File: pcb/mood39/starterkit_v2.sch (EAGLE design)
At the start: 19 parts, among them IC1 TINY85, IC2 LP2950

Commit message: new usb connector package
this will be puzzling not fun :-/
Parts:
- U$2: value USB_B -> USB_BS; device n39:USB_B -> n39:USB_BS
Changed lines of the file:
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@@
 <grid distance="0.1" unitdist="inch" unit="inch" style="lines" multiple="1" display="no" altdistance="0.01" altunitdist="inch" altunit="inch"/>
 <layers>
-<layer number="1" name="Top" color="4" fill="1" visible="no" active="no"/>
-<layer number="16" name="Bottom" color="1" fill="1" visible="no" active="no"/>
-<layer number="17" name="Pads" color="2" fill="1" visible="no" active="no"/>
-<layer number="18" name="Vias" color="2" fill="1" visible="no" active="no"/>
-<layer number="19" name="Unrouted" color="6" fill="1" visible="no" active="no"/>
-<layer number="20" name="Dimension" color="15" fill="1" visible="no" active="no"/>
-<layer number="21" name="tPlace" color="7" fill="1" visible="no" active="no"/>
-<layer number="22" name="bPlace" color="7" fill="1" visible="no" active="no"/>
-<layer number="23" name="tOrigins" color="15" fill="1" visible="no" active="no"/>
-<layer number="24" name="bOrigins" color="15" fill="1" visible="no" active="no"/>
-<layer number="25" name="tNames" color="7" fill="1" visible="no" active="no"/>
-<layer number="26" name="bNames" color="7" fill="1" visible="no" active="no"/>
-<layer number="27" name="tValues" color="7" fill="1" visible="no" active="no"/>
-<layer number="28" name="bValues" color="7" fill="1" visible="no" active="no"/>
+<layer number="1" name="Top" color="4" fill="1" visible="yes" active="no"/>
+<layer number="16" name="Bottom" color="1" fill="1" visible="yes" active="no"/>
+<layer number="17" name="Pads" color="2" fill="1" visible="yes" active="no"/>
+<layer number="18" name="Vias" color="2" fill="1" visible="yes" active="no"/>
+<layer number="19" name="Unrouted" color="6" fill="1" visible="yes" active="no"/>
+<layer number="20" name="Dimension" color="15" fill="1" visible="yes" active="no"/>
+<layer number="21" name="tPlace" color="7" fill="1" visible="yes" active="no"/>
+<layer number="22" name="bPlace" color="7" fill="1" visible="yes" active="no"/>
+<layer number="23" name="tOrigins" color="15" fill="1" visible="yes" active="no"/>
+<layer number="24" name="bOrigins" color="15" fill="1" visible="yes" active="no"/>
+<layer number="25" name="tNames" color="7" fill="1" visible="yes" active="no"/>
+<layer number="26" name="bNames" color="7" fill="1" visible="yes" active="no"/>
+<layer number="27" name="tValues" color="7" fill="1" visible="yes" active="no"/>
+<layer number="28" name="bValues" color="7" fill="1" visible="yes" active="no"/>
 <layer number="29" name="tStop" color="7" fill="3" visible="no" active="no"/>
 <layer number="30" name="bStop" color="7" fill="6" visible="no" active="no"/>
@@
 <layer number="35" name="tGlue" color="7" fill="4" visible="no" active="no"/>
 <layer number="36" name="bGlue" color="7" fill="5" visible="no" active="no"/>
-<layer number="37" name="tTest" color="7" fill="1" visible="no" active="no"/>
-<layer number="38" name="bTest" color="7" fill="1" visible="no" active="no"/>
+<layer number="37" name="tTest" color="7" fill="1" visible="yes" active="no"/>
+<layer number="38" name="bTest" color="7" fill="1" visible="yes" active="no"/>
 <layer number="39" name="tKeepout" color="4" fill="11" visible="no" active="no"/>
 <layer number="40" name="bKeepout" color="1" fill="11" visible="no" active="no"/>
@@
 <layer number="44" name="Drills" color="7" fill="1" visible="no" active="no"/>
 <layer number="45" name="Holes" color="7" fill="1" visible="no" active="no"/>
-<layer number="46" name="Milling" color="3" fill="1" visible="no" active="no"/>
-<layer number="47" name="Measures" color="7" fill="1" visible="no" active="no"/>
-<layer number="48" name="Document" color="7" fill="1" visible="no" active="no"/>
-<layer number="49" name="Reference" color="7" fill="1" visible="no" active="no"/>
-<layer number="51" name="tDocu" color="7" fill="1" visible="no" active="no"/>
-<layer number="52" name="bDocu" color="7" fill="1" visible="no" active="no"/>
+<layer number="46" name="Milling" color="3" fill="1" visible="yes" active="no"/>
+<layer number="47" name="Measures" color="7" fill="1" visible="yes" active="no"/>
+<layer number="48" name="Document" color="7" fill="1" visible="yes" active="no"/>
+<layer number="49" name="Reference" color="7" fill="1" visible="yes" active="no"/>
+<layer number="51" name="tDocu" color="7" fill="1" visible="yes" active="no"/>
+<layer number="52" name="bDocu" color="7" fill="1" visible="yes" active="no"/>
 <layer number="91" name="Nets" color="2" fill="1" visible="yes" active="yes"/>
 <layer number="92" name="Busses" color="1" fill="1" visible="yes" active="yes"/>
@@
 <part name="JP2" library="pinhead" deviceset="PINHD-1X1" device=""/>
 <part name="JP3" library="pinhead" deviceset="PINHD-1X1" device=""/>
-<part name="U$2" library="n39" deviceset="USB_B" device=""/>
+<part name="U$2" library="n39" deviceset="USB_B" device="S" value="USB_BS"/>
 </parts>
 <sheets>

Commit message: start routing
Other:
- moved on the sheet: JP2, JP3
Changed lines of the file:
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@@
 <instance part="S1" gate="S$1" x="73.66" y="50.8" rot="R270"/>
 <instance part="U$1" gate="G$1" x="-30.48" y="88.9" rot="R180"/>
-<instance part="JP2" gate="G$1" x="132.08" y="25.4"/>
-<instance part="JP3" gate="G$1" x="132.08" y="38.1"/>
+<instance part="JP2" gate="G$1" x="132.08" y="22.86"/>
+<instance part="JP3" gate="G$1" x="132.08" y="30.48"/>
 <instance part="U$2" gate="G$1" x="93.98" y="30.48"/>
 </instances>
@@
 </segment>
 <segment>
-<wire x1="106.68" y1="35.56" x2="116.84" y2="35.56" width="0.1524" layer="91"/>
-<label x="109.22" y="35.56" size="1.778" layer="95"/>
+<label x="129.54" y="40.64" size="1.778" layer="95"/>
+<wire x1="111.76" y1="40.64" x2="111.76" y2="35.56" width="0.1524" layer="91"/>
 <pinref part="U$2" gate="G$1" pin="VBUS"/>
+<wire x1="111.76" y1="35.56" x2="106.68" y2="35.56" width="0.1524" layer="91"/>
+<wire x1="111.76" y1="40.64" x2="119.38" y2="40.64" width="0.1524" layer="91"/>
+<wire x1="121.92" y1="40.64" x2="137.16" y2="40.64" width="0.1524" layer="91"/>
+<wire x1="121.92" y1="40.64" x2="119.38" y2="40.64" width="0.1524" layer="91"/>
 </segment>
 </net>
@@
 <net name="USBD-" class="0">
 <segment>
-<wire x1="106.68" y1="33.02" x2="121.92" y2="33.02" width="0.1524" layer="91"/>
+<wire x1="106.68" y1="33.02" x2="124.46" y2="33.02" width="0.1524" layer="91"/>
+<wire x1="124.46" y1="33.02" x2="124.46" y2="30.48" width="0.1524" layer="91"/>
+<wire x1="124.46" y1="30.48" x2="129.54" y2="30.48" width="0.1524" layer="91"/>
 <label x="109.22" y="33.02" size="1.778" layer="95"/>
 <pinref part="JP3" gate="G$1" pin="1"/>
-<wire x1="129.54" y1="38.1" x2="121.92" y2="38.1" width="0.1524" layer="91"/>
-<wire x1="121.92" y1="38.1" x2="121.92" y2="33.02" width="0.1524" layer="91"/>
 <pinref part="U$2" gate="G$1" pin="D-"/>
 </segment>
@@
 <segment>
 <wire x1="106.68" y1="30.48" x2="121.92" y2="30.48" width="0.1524" layer="91"/>
-<wire x1="121.92" y1="30.48" x2="121.92" y2="25.4" width="0.1524" layer="91"/>
-<wire x1="121.92" y1="25.4" x2="129.54" y2="25.4" width="0.1524" layer="91"/>
+<wire x1="121.92" y1="30.48" x2="121.92" y2="22.86" width="0.1524" layer="91"/>
+<wire x1="121.92" y1="22.86" x2="129.54" y2="22.86" width="0.1524" layer="91"/>
 <label x="109.22" y="30.48" size="1.778" layer="95"/>
 <pinref part="JP2" gate="G$1" pin="1"/>

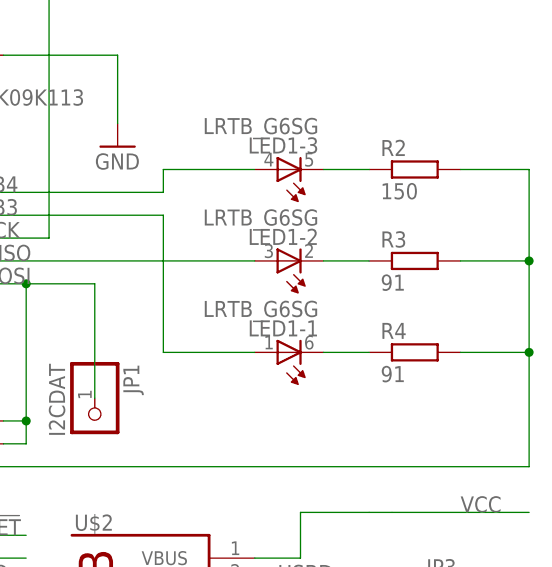
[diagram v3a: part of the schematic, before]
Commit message: adapt resitor values and add git ignore list
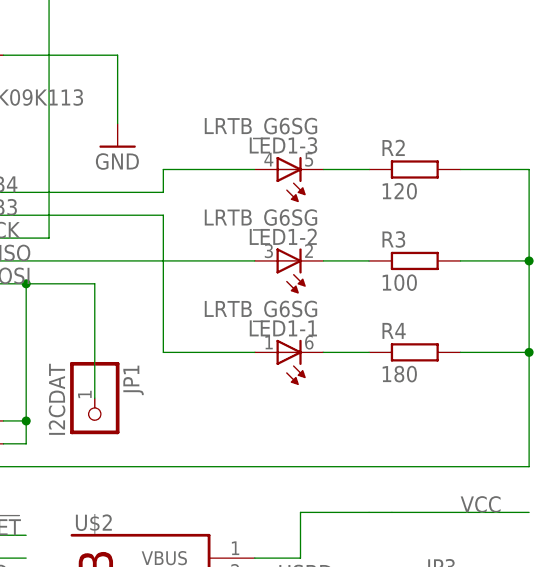
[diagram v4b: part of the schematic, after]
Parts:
- R2: value 150 -> 120
- R3: value 91 -> 100
- R4: value 91 -> 180
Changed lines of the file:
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@@
 <part name="P+1" library="supply1" deviceset="VCC" device=""/>
 <part name="R1" library="rcl" deviceset="R-EU_" device="R0805" value="10k"/>
-<part name="R2" library="rcl" deviceset="R-EU_" device="R0805" value="150"/>
-<part name="R3" library="rcl" deviceset="R-EU_" device="R0805" value="91"/>
-<part name="R4" library="rcl" deviceset="R-EU_" device="R0805" value="91"/>
+<part name="R2" library="rcl" deviceset="R-EU_" device="R0805" value="120"/>
+<part name="R3" library="rcl" deviceset="R-EU_" device="R0805" value="100"/>
+<part name="R4" library="rcl" deviceset="R-EU_" device="R0805" value="180"/>
 <part name="SV1" library="con-ml" deviceset="ML6" device="" value="ISP"/>
 <part name="IC2" library="v-reg" deviceset="LP2950?*" device="ACZ" technology="-5.0" value="LP2950"/>

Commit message: value for potentiometer
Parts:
- R5: value ALPS_RK09K113 -> 100k
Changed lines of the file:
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@@
 <part name="IC2" library="v-reg" deviceset="LP2950?*" device="ACZ" technology="-5.0" value="LP2950"/>
 <part name="C2" library="rcl" deviceset="CPOL-EU" device="E2-5" value="2.2u"/>
-<part name="R5" library="n39" deviceset="ALPS_RK09K113" device=""/>
+<part name="R5" library="n39" deviceset="ALPS_RK09K113" device="" value="100k"/>
 <part name="JP1" library="pinhead" deviceset="PINHD-1X1" device="" value="I2CDAT"/>
 <part name="GND2" library="supply1" deviceset="GND" device=""/>
